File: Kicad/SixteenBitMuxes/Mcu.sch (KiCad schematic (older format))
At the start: 18 parts, among them J10 JST XH Buttons, J11 LCD JST XH, J12 Bypass Switch JST XH, J7 Boot Reset PinHeader, J9 SWD_PinHeader, U3 STM32F103C8Tx, Y1 8MHz

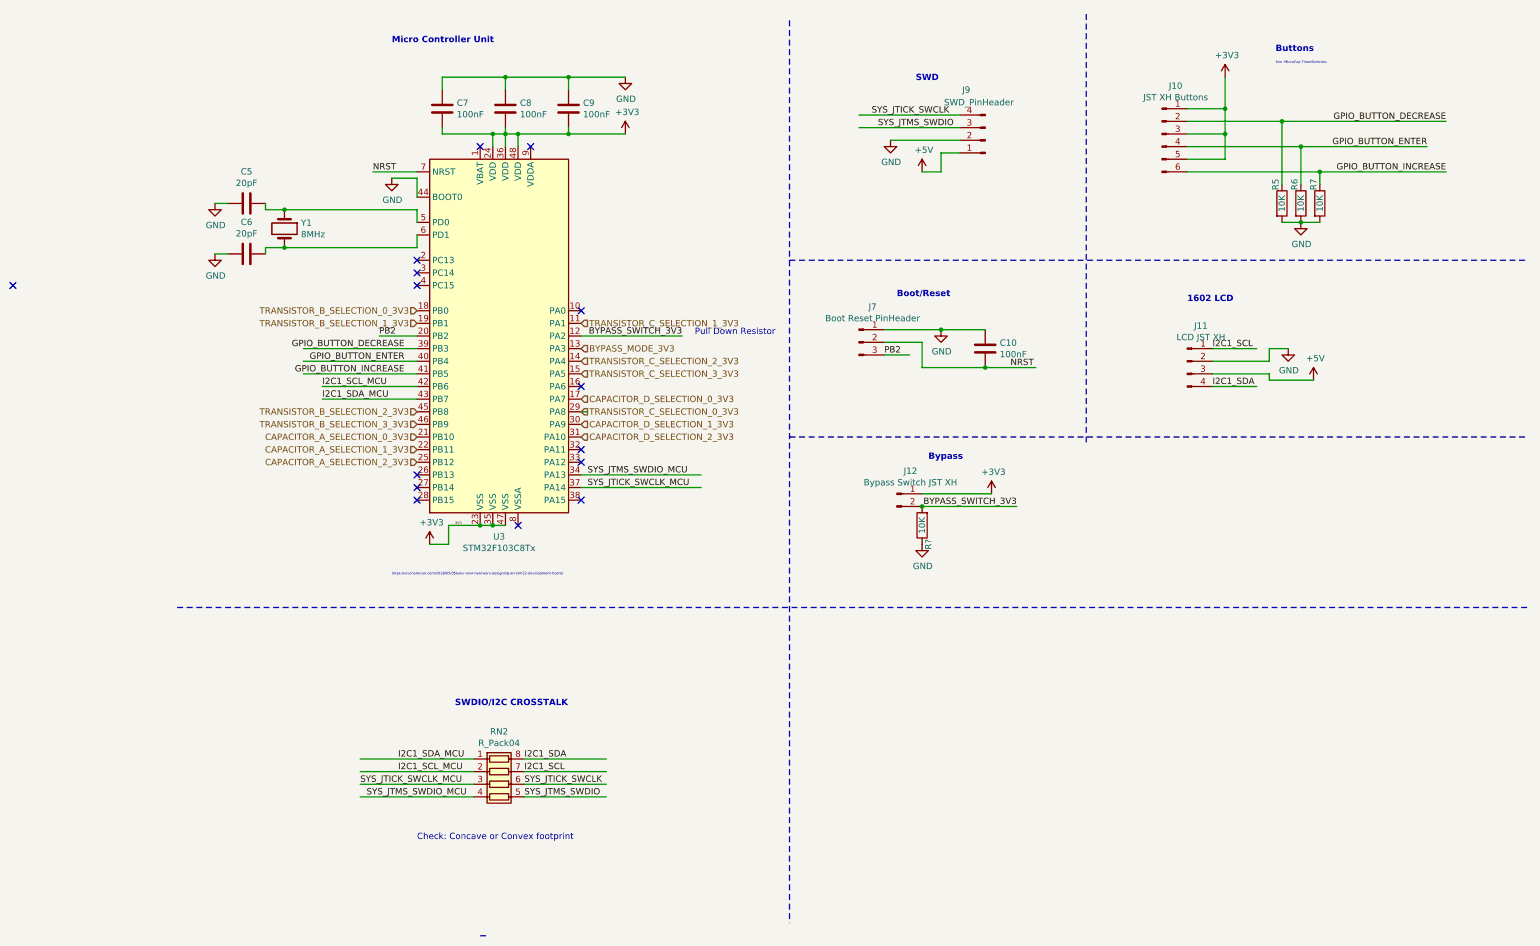
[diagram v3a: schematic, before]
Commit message: Code + resistors
Many code changes (UI) + resistors -> pulldowns.
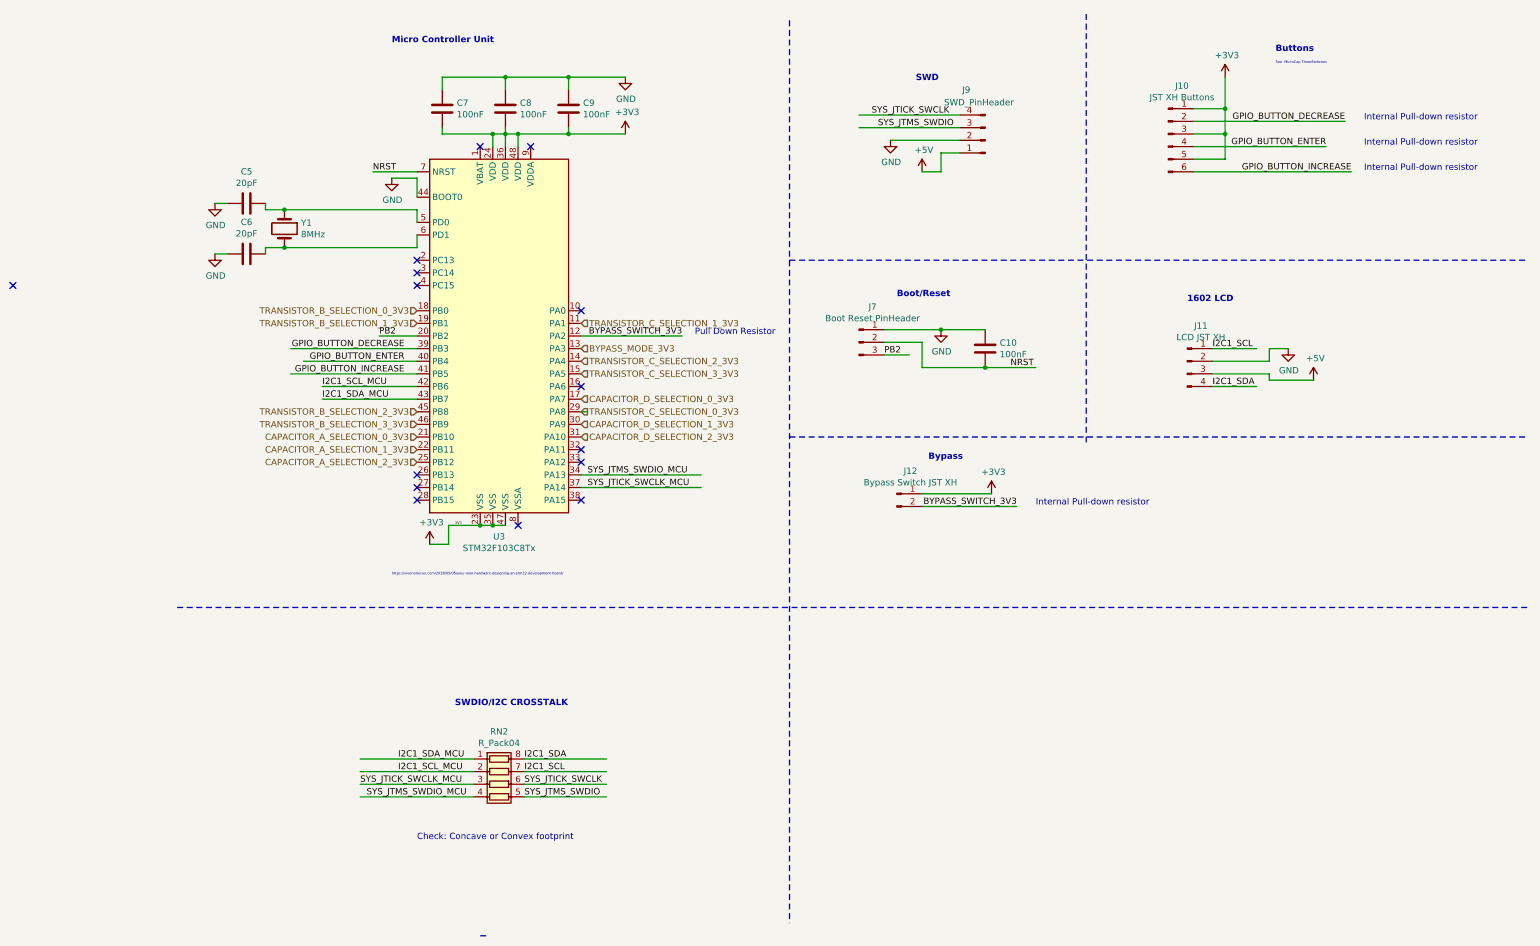
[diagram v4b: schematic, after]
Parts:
- removed R5, R6, R7, R?: 10K, Resistor_SMD:R_0805_2012Metric_Pad1.15x1.40mm_HandSolder, symbol Device:R
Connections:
- wire segments 93 -> 85
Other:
- note added: "Internal Pull-down resistor"
- moved on the sheet: J10
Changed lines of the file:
@@
 	5350 550  5350 7700
-$Comp
-L Device:R R?
-U 1 1 5EA32EA7
-P 9550 2000
-AR Path="/5EA32EA7" Ref="R?"  Part="1"
-AR Path="/5E8F7778/5EA32EA7" Ref="R?"  Part="1"
-AR Path="/5E8BDF21/5EA32EA7" Ref="R7"  Part="1"
-F 0 "R7" V 9500 2150 50  0000 C CNN
-F 1 "10K" V 9550 2000 50  0000 C CNN
-F 2 "Resistor_SMD:R_0805_2012Metric_Pad1.15x1.40mm_HandSolder" V 9480 2000 50  0001 C CNN
-F 3 "~" H 9550 2000 50  0001 C CNN
-	1    9550 2000
-	1    0    0    -1
-$EndComp
-$Comp
-L Device:R R?
-U 1 1 5EA32EAD
-P 9400 2000
-AR Path="/5EA32EAD" Ref="R?"  Part="1"
-AR Path="/5E8F7778/5EA32EAD" Ref="R?"  Part="1"
-AR Path="/5E8BDF21/5EA32EAD" Ref="R6"  Part="1"
-F 0 "R6" V 9350 2150 50  0000 C CNN
-F 1 "10K" V 9400 2000 50  0000 C CNN
-F 2 "Resistor_SMD:R_0805_2012Metric_Pad1.15x1.40mm_HandSolder" V 9330 2000 50  0001 C CNN
-F 3 "~" H 9400 2000 50  0001 C CNN
-	1    9400 2000
-	1    0    0    -1
-$EndComp
-$Comp
-L Device:R R?
-U 1 1 5EA32EB3
-P 9250 2000
-AR Path="/5EA32EB3" Ref="R?"  Part="1"
-AR Path="/5E8F7778/5EA32EB3" Ref="R?"  Part="1"
-AR Path="/5E8BDF21/5EA32EB3" Ref="R5"  Part="1"
-F 0 "R5" V 9200 2150 50  0000 C CNN
-F 1 "10K" V 9250 2000 50  0000 C CNN
-F 2 "Resistor_SMD:R_0805_2012Metric_Pad1.15x1.40mm_HandSolder" V 9180 2000 50  0001 C CNN
-F 3 "~" H 9250 2000 50  0001 C CNN
-	1    9250 2000
-	1    0    0    -1
-$EndComp
 $Comp
 L power:GND #PWR?
@@
 Wire Wire Line
 	8700 3350 9150 3350
-Text Label 10400 1550 2    50   ~ 0
+Text Label 9600 1550 2    50   ~ 0
 GPIO_BUTTON_ENTER
-Text Label 10550 1750 2    50   ~ 0
+Text Label 9800 1750 2    50   ~ 0
 GPIO_BUTTON_INCREASE
 Wire Notes Line
@@
 	3700 3050 4500 3050
 Wire Wire Line
-	2400 3350 1500 3350
+	2400 3350 1400 3350
 Wire Wire Line
 	1500 3250 2400 3250
 Wire Wire Line
-	2400 3150 1500 3150
+	2400 3150 1400 3150
 Text Label 2300 3350 2    50   ~ 0
 GPIO_BUTTON_INCREASE
@@
 L Connector:Conn_01x06_Male J10
 U 1 1 5ECC424B
-P 8300 1450
-F 0 "J10" H 8408 1831 50  0000 C CNN
-F 1 "JST XH Buttons" H 8408 1740 50  0000 C CNN
-F 2 "Connector_JST:JST_XH_B6B-XH-A_1x06_P2.50mm_Vertical" H 8300 1450 50  0001 C CNN
-F 3 "~" H 8300 1450 50  0001 C CNN
-	1    8300 1450
-	1    0    0    -1
-$EndComp
-Text Label 10550 1350 2    50   ~ 0
+P 8350 1450
+F 0 "J10" H 8458 1831 50  0000 C CNN
+F 1 "JST XH Buttons" H 8458 1740 50  0000 C CNN
+F 2 "Connector_JST:JST_XH_B6B-XH-A_1x06_P2.50mm_Vertical" H 8350 1450 50  0001 C CNN
+F 3 "~" H 8350 1450 50  0001 C CNN
+	1    8350 1450
+	1    0    0    -1
+$EndComp
+Text Label 9750 1350 2    50   ~ 0
 GPIO_BUTTON_DECREASE
-Connection ~ 9250 1350
-Wire Wire Line
-	9250 1350 10550 1350
-Wire Wire Line
-	9400 1550 10400 1550
-Connection ~ 9400 1550
-Wire Wire Line
-	9550 1750 10550 1750
-Connection ~ 9550 1750
 $Comp
 L power:+3V3 #PWR023
@@
 $EndComp
 Wire Wire Line
-	8500 1350 9250 1350
-Wire Wire Line
-	8500 1550 9400 1550
-Wire Wire Line
-	8500 1750 9550 1750
-Wire Wire Line
-	8500 1650 8800 1650
+	8550 1650 8800 1650
 Wire Wire Line
 	8800 1650 8800 1450
 Wire Wire Line
-	8500 1450 8800 1450
+	8550 1450 8800 1450
 Connection ~ 8800 1450
 Wire Wire Line
 	8800 1450 8800 1250
 Wire Wire Line
-	8500 1250 8800 1250
+	8550 1250 8800 1250
 Connection ~ 8800 1250
 Wire Wire Line
@@
 Wire Notes Line
 	500  5200 11200 5200
-$Comp
-L power:GND #PWR0118
-U 1 1 5EE03286
-P 9400 2150
-F 0 "#PWR0118" H 9400 1900 50  0001 C CNN
-F 1 "GND" H 9405 1977 50  0000 C CNN
-F 2 "" H 9400 2150 50  0001 C CNN
-F 3 "" H 9400 2150 50  0001 C CNN
-	1    9400 2150
-	1    0    0    -1
-$EndComp
 Text HLabel 3700 3150 2    50   Input ~ 0
 BYPASS_MODE_3V3
-$Comp
-L Device:R R?
-U 1 1 5EE7BBB4
-P 6400 4550
-AR Path="/5EE7BBB4" Ref="R?"  Part="1"
-AR Path="/5E8F7778/5EE7BBB4" Ref="R?"  Part="1"
-AR Path="/5E8BDF21/5EE7BBB4" Ref="R?"  Part="1"
-F 0 "R?" V 6350 4700 50  0000 C CNN
-F 1 "10K" V 6400 4550 50  0000 C CNN
-F 2 "Resistor_SMD:R_0805_2012Metric_Pad1.15x1.40mm_HandSolder" V 6330 4550 50  0001 C CNN
-F 3 "~" H 6400 4550 50  0001 C CNN
-	1    6400 4550
-	-1   0    0    1
-$EndComp
-$Comp
-L power:GND #PWR?
-U 1 1 5EE7BBBA
-P 6400 4700
-F 0 "#PWR?" H 6400 4450 50  0001 C CNN
-F 1 "GND" H 6405 4527 50  0000 C CNN
-F 2 "" H 6400 4700 50  0001 C CNN
-F 3 "" H 6400 4700 50  0001 C CNN
-	1    6400 4700
-	1    0    0    -1
-$EndComp
-Connection ~ 6400 4400
-Wire Wire Line
-	9550 1750 9550 1850
-Wire Wire Line
-	9400 1850 9400 1550
-Wire Wire Line
-	9250 1850 9250 1350
-Wire Wire Line
-	9250 2150 9400 2150
-Connection ~ 9400 2150
-Wire Wire Line
-	9400 2150 9550 2150
 Text Notes 9200 1050 0    50   ~ 10
 Buttons\n\n\n\n
+Text Notes 7300 4400 0    50   ~ 0
+Internal Pull-down resistor
+Wire Wire Line
+	8550 1350 9750 1350
+Wire Wire Line
+	8550 1550 9600 1550
+Wire Wire Line
+	8550 1750 9800 1750
+Text Notes 9900 1350 0    50   ~ 0
+Internal Pull-down resistor
+Text Notes 9900 1550 0    50   ~ 0
+Internal Pull-down resistor
+Text Notes 9900 1750 0    50   ~ 0
+Internal Pull-down resistor
 $EndSCHEMATC

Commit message: Improvements according video youtube
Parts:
- removed J9: SWD_PinHeader, Connector_PinHeader_2.54mm:PinHeader_1x04_P2.54mm_Vertical, symbol Connector:Conn_01x04_Male
- added C20: 10uF, Capacitor_SMD:C_0805_2012Metric_Pad1.15x1.40mm_HandSolder, symbol Device:C
- added J9: SWD PinHeader, Connector_PinHeader_2.54mm:PinHeader_1x05_P2.54mm_Vertical, symbol Connector:Conn_01x05_Male
- added R5: 220R, Resistor_SMD:R_0805_2012Metric_Pad1.15x1.40mm_HandSolder, symbol Device:R
- added R6, R7: 10K, Resistor_SMD:R_0805_2012Metric_Pad1.15x1.40mm_HandSolder, symbol Device:R
- Y1: footprint Crystal:Crystal_HC49-U_Vertical -> Crystal:Crystal_HC49-4H_Vertical
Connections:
- net labels added: BOOT1, MCU_BYPASS_CAPS, OSC_IN, OSC_OUT, SYS_JTDO_TRACESWO
- wire segments 85 -> 95
- no-connect marks 15 -> 12
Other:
- note added: "Cl = 2 * (CLOAD_CRYSTAL - CPARASITIC)\n (for STM32F405...)\n = 2 * (9pF - 2pF) = 14 pF \n(see YouTube: KiCad STM32 Hardware Design \nand JLCPCB Assembly)\n"
- note added: "Micro Controller Unit Bypass Capacitors\n\n\n\n"
- note added: "Oscillator\n\n\n"
- note added: "Resistor for driving less and\nremoving high frequenties\n(see same YouTube video\nas above)"
- note added: "f(-3dB) = 1/(2*pi*C*R)\n= 16 MHz * 2 * pi * 9 pF * R) = 1 <=> R ="
- moved on the sheet: C5, C6, C7, C8, C9, J12, RN2, Y1

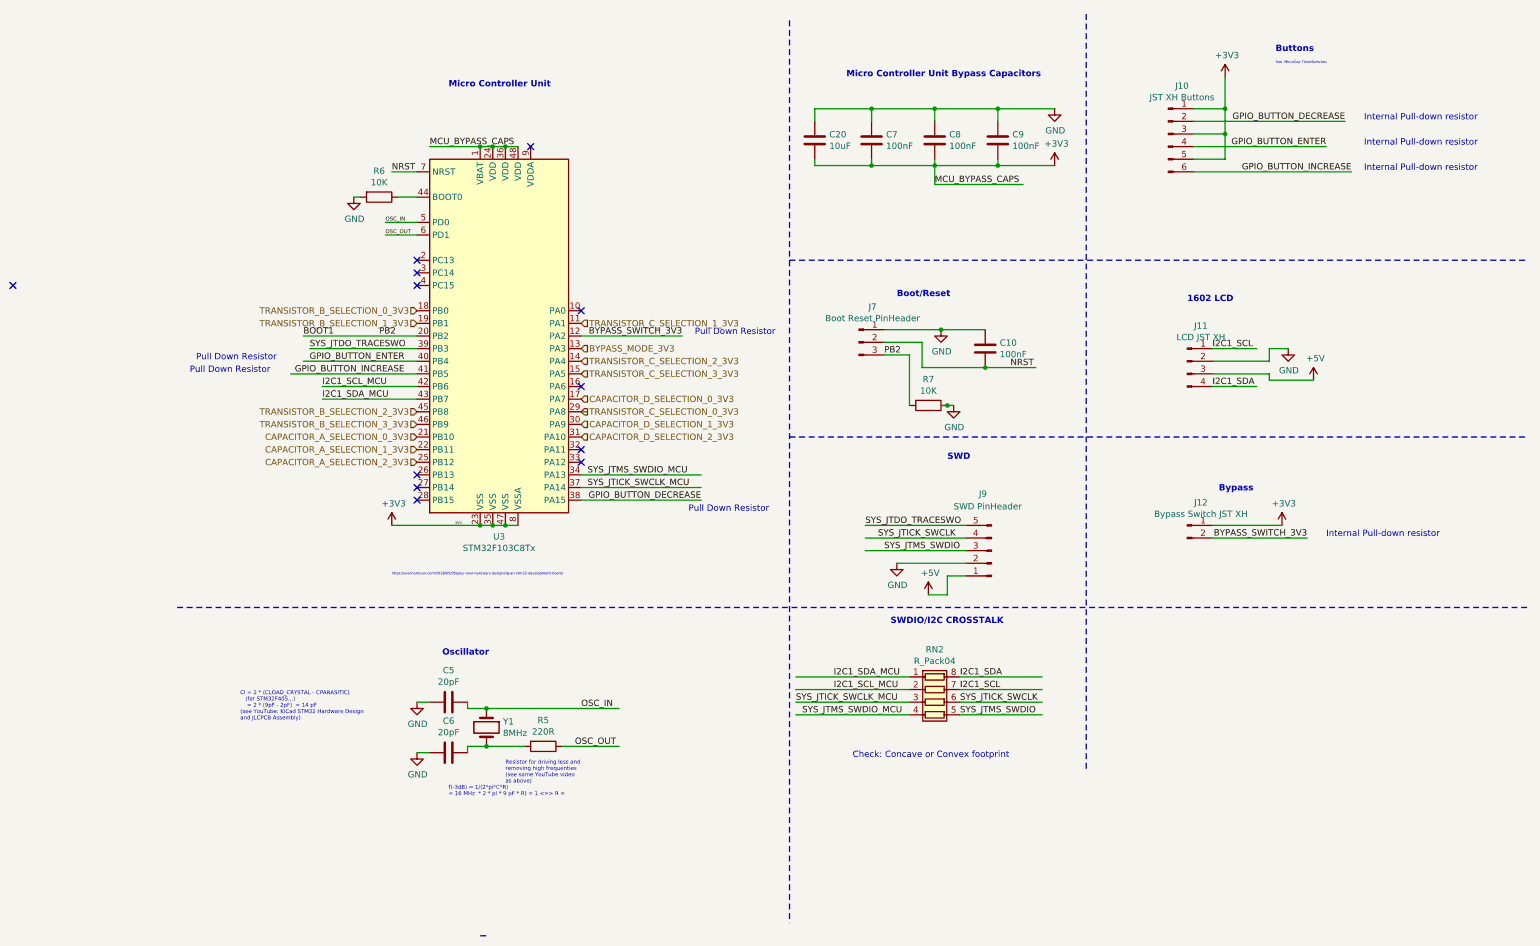
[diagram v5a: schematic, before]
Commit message: UART, BOOT, NRST, Isolated OSC gnd
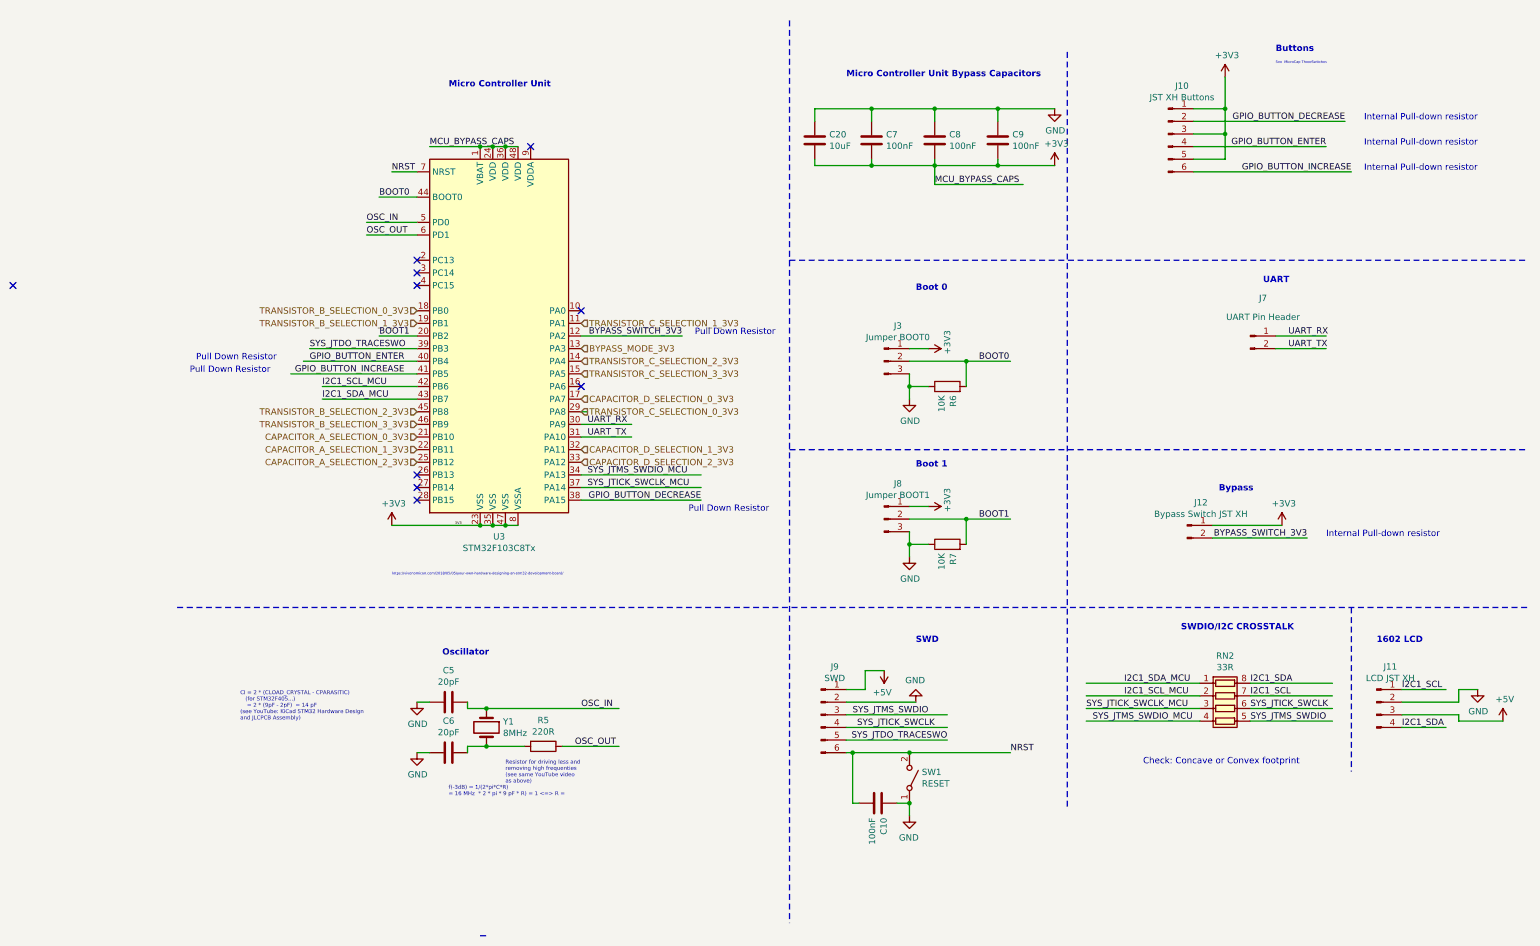
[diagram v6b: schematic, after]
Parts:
- removed J7: Boot Reset PinHeader, Connector_PinHeader_2.54mm:PinHeader_1x03_P2.54mm_Vertical, symbol Connector:Conn_01x03_Male
- removed J9: SWD PinHeader, Connector_PinHeader_2.54mm:PinHeader_1x05_P2.54mm_Vertical, symbol Connector:Conn_01x05_Male
- added J3: Jumper BOOT0, Connector_PinHeader_2.54mm:PinHeader_1x03_P2.54mm_Vertical, symbol Connector:Conn_01x03_Male
- added J7: UART Pin Header, Connector_PinHeader_2.54mm:PinHeader_1x02_P2.54mm_Vertical, symbol Connector:Conn_01x02_Male
- added J8: Jumper BOOT1, Connector_PinHeader_2.54mm:PinHeader_1x03_P2.54mm_Vertical, symbol Connector:Conn_01x03_Male
- added J9: SWD, Connector_PinHeader_2.54mm:PinHeader_1x06_P2.54mm_Vertical, symbol Connector:Conn_01x06_Male
- added SW1: RESET, Button_Switch_SMD:SW_SPST_CK_RS282G05A3, symbol Switch:SW_SPST
- RN2: value R_Pack04 -> 33R
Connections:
- net labels added: BOOT0, UART_RX, UART_TX
- net labels removed: PB2
- wire segments 95 -> 109
- no-connect marks 12 -> 10
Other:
- note added: "Boot 0\n"
- note added: "Boot 1\n"
- note added: "UART\n\n\n"
- note removed: "Boot/Reset\n"
- moved on the sheet: C10, J11, R6, R7, RN2

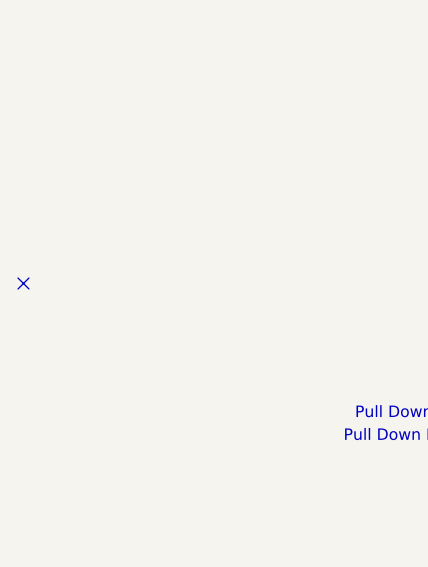
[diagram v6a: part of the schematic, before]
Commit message: STM32 DevBoard in Freecad
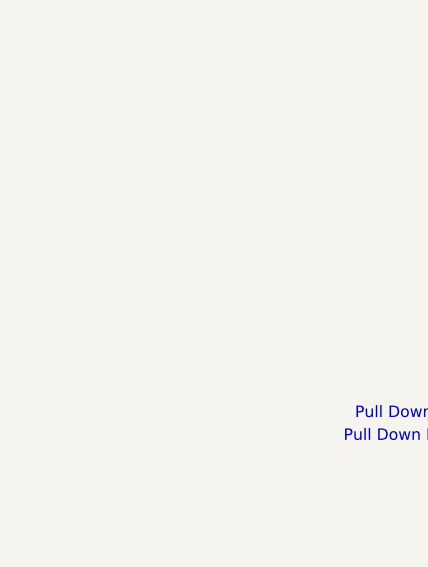
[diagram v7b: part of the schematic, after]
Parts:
- U3: footprint Package_QFP:LQFP-48_7x7mm_P0.5mm -> Package_QFP:LQFP-48-1EP_7x7mm_P0.5mm_EP3.6x3.6mm_ThermalVias
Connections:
- no-connect marks 10 -> 9
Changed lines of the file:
@@
 F 0 "U3" H 3050 1461 50  0000 C CNN
 F 1 "STM32F103C8Tx" H 3050 1370 50  0000 C CNN
-F 2 "Package_QFP:LQFP-48_7x7mm_P0.5mm" H 2500 1650 50  0001 R CNN
+F 2 "Package_QFP:LQFP-48-1EP_7x7mm_P0.5mm_EP3.6x3.6mm_ThermalVias" H 2500 1650 50  0001 R CNN
 F 3 "http://www.st.com/st-web-ui/static/active/en/resource/technical/document/datasheet/CD00161566.pdf" H 3100 3050 50  0001 C CNN
 	1    3100 3050
@@
 Wire Wire Line
 	8700 4650 9450 4650
-NoConn ~ -800 2650
 $Comp
 L Connector:Conn_01x06_Male J10
